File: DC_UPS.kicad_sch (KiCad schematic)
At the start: 32 parts, among them J1 USB_B_Micro, J2 POWER, J3 STATUS, Q1 SIS402DN, Q2 SIS402DN, U1 LTC4040

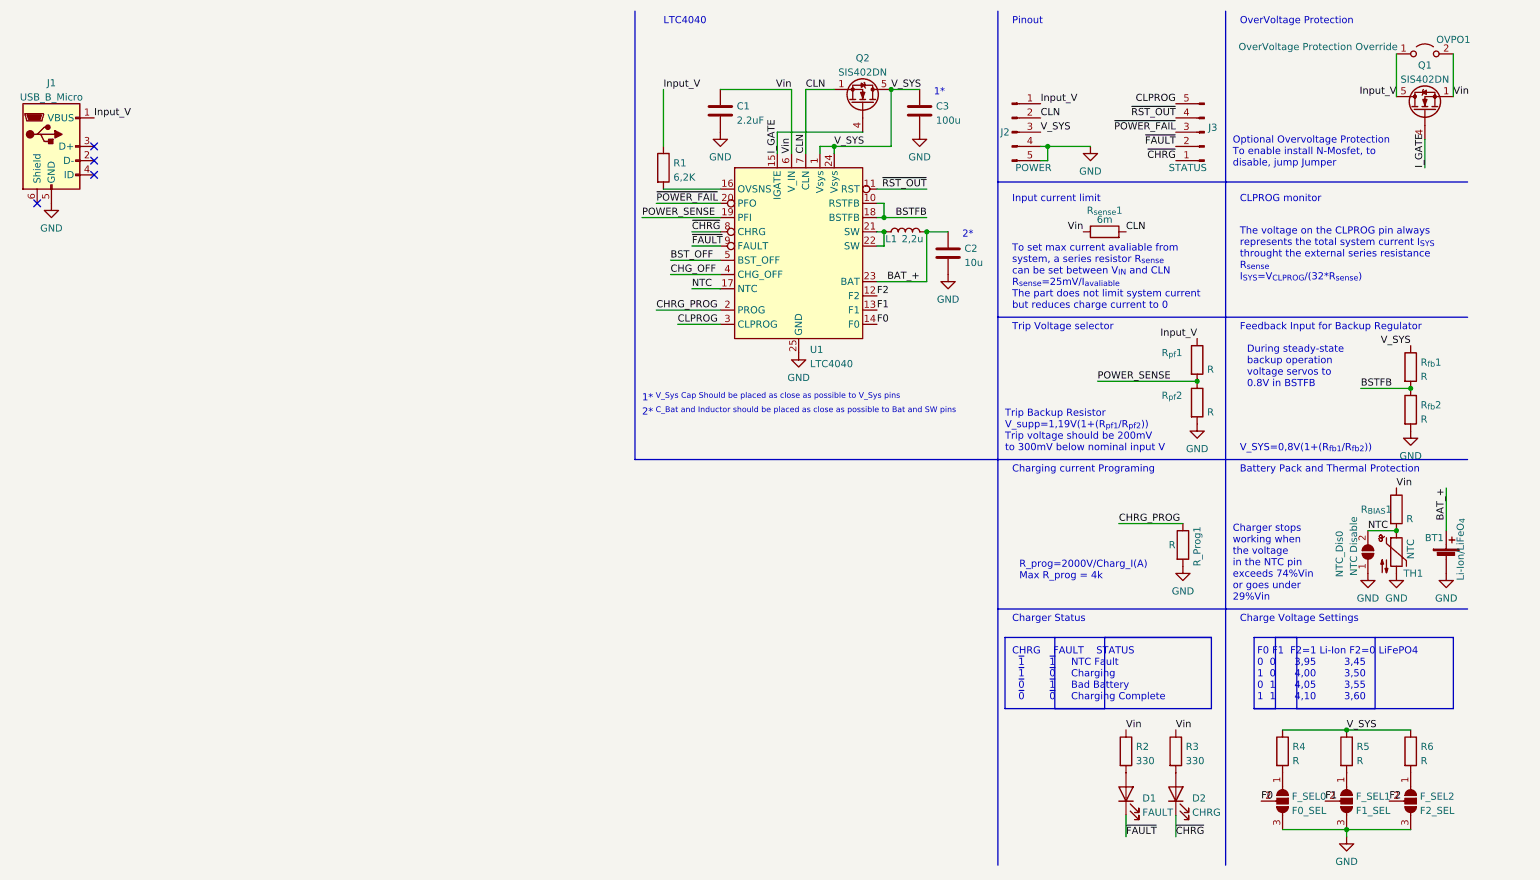
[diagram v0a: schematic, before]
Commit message: [Board]Build board without connectors
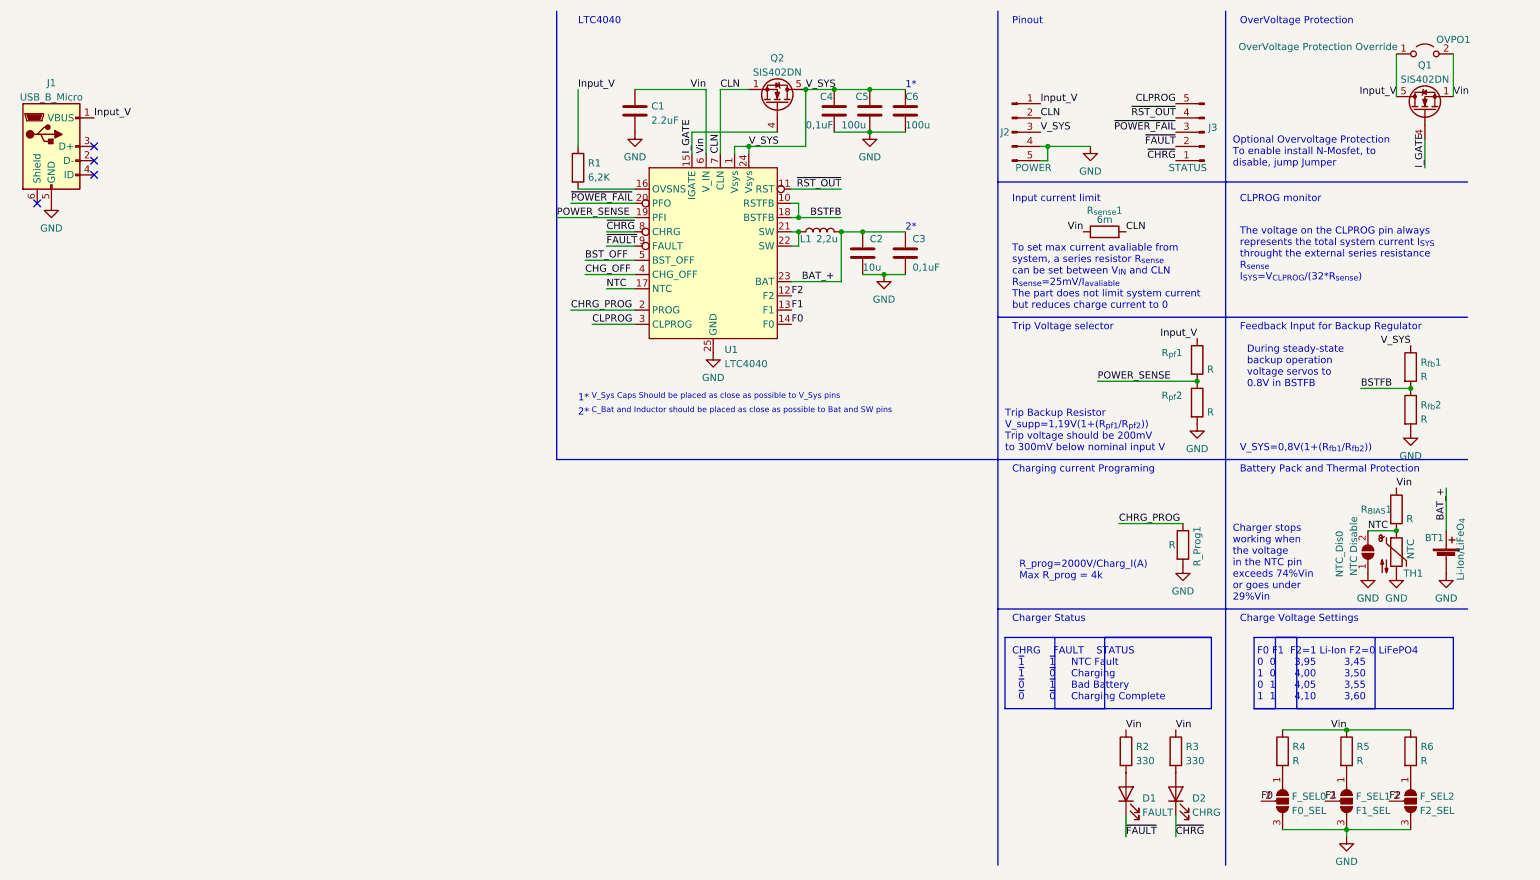
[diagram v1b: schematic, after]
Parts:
- added C3, C4: 0,1uF, Capacitor_SMD:C_0402_1005Metric_Pad0.74x0.62mm_HandSolder, symbol Device:C
- added C6: 100u, Capacitor_SMD:C_1206_3216Metric_Pad1.33x1.80mm_HandSolder, symbol Device:C
- renumbered C3 to C5
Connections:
- net BAT_+: now also C3.1
- net GND: now also C3.2, C4.2, C6.2
- net V_SYS: now also C4.1, C6.1; no longer R4.1, R5.1, R6.1
- net Vin: now also R4.1, R5.1, R6.1
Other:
- note added: "1*^{ V_Sys Caps Should be placed as close as possible to V_Sys pins}"
- note removed: "1*^{ V_Sys Cap Should be placed as close as possible to V_Sys pins}"
- moved on the sheet: C1, C2, C5, L1, Q2, R1, U1

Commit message: [Board]Finish product rev 1
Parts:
- added J4: BAT_CONN, Connector_JST:JST_SH_BM03B-SRSS-TB_1x03-1MP_P1.00mm_Vertical, symbol Connector:Conn_01x03_Female
- BT1: footprint Battery:BatteryHolder_Keystone_1042_1x18650 -> TE:TE_1776119-2
- J2, J3: footprint Connector_PinSocket_2.54mm:PinSocket_1x05_P2.54mm_Vertical -> Castellated_Header:CastellatedPinHeader_2.54mm_5
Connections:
- net BAT_+: now also J4.1 (Pin_1)
- net CLPROG: now also J3.4 (Pin_4); no longer J3.5 (Pin_5)
- net GND: now also J4.3 (Pin_3)
- net NTC: now also J4.2 (Pin_2)
- net ~{CHRG}: now also J3.2 (Pin_2); no longer J3.1 (Pin_1)
- net ~{FAULT}: now also J3.1 (Pin_1); no longer J3.2 (Pin_2)
- net ~{POWER_FAIL}: now also J3.5 (Pin_5); no longer J3.3 (Pin_3)
- net ~{RST_OUT}: now also J3.3 (Pin_3); no longer J3.4 (Pin_4)
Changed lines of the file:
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@@
+    (stroke (width 0) (type default) (color 0 0 0 0))
+  )
+  (wire (pts (xy 257.81 102.87) (xy 259.08 102.87))
     (stroke (width 0) (type default) (color 0 0 0 0))
   )
@@
     (effects (font (size 1.27 1.27)) (justify left bottom))
   )
-  (label "CLPROG" (at 232.41 29.21 180)
+  (label "CLPROG" (at 232.41 31.75 180)
     (effects (font (size 1.27 1.27)) (justify right bottom))
   )
@@
     (effects (font (size 1.27 1.27)) (justify left bottom))
   )
+  (label "NTC" (at 257.81 100.33 0)
+    (effects (font (size 1.27 1.27)) (justify left bottom))
+  )
+  (label "BAT_+" (at 257.81 97.79 0)
+    (effects (font (size 1.27 1.27)) (justify left bottom))
+  )
   (label "CLPROG" (at 128.27 68.58 0)
     (effects (font (size 1.27 1.27)) (justify left bottom))
@@
     (effects (font (size 1.27 1.27)) (justify left bottom))
   )
-  (label "~{CHRG}" (at 232.41 39.37 180)
+  (label "~{CHRG}" (at 232.41 36.83 180)
     (effects (font (size 1.27 1.27)) (justify right bottom))
   )
@@
     (effects (font (size 1.27 1.27)) (justify right bottom))
   )
-  (label "~{FAULT}" (at 232.41 36.83 180)
+  (label "~{FAULT}" (at 232.41 39.37 180)
     (effects (font (size 1.27 1.27)) (justify right bottom))
   )
@@
     (effects (font (size 1.27 1.27)) (justify left bottom))
   )
-  (label "~{POWER_FAIL}" (at 232.41 34.29 180)
+  (label "~{POWER_FAIL}" (at 232.41 29.21 180)
     (effects (font (size 1.27 1.27)) (justify right bottom))
   )
@@
     (effects (font (size 1.27 1.27)) (justify right bottom))
   )
-  (label "~{RST_OUT}" (at 232.41 31.75 180)
+  (label "~{RST_OUT}" (at 232.41 34.29 180)
     (effects (font (size 1.27 1.27)) (justify right bottom))
   )
@@
       (effects (font (size 1.27 1.27)) (justify left))
     )
-    (property "Footprint" "Battery:BatteryHolder_Keystone_1042_1x18650" (id 2) (at 280.67 108.966 90)
+    (property "Footprint" "TE:TE_1776119-2" (id 2) (at 280.67 108.966 90)
       (effects (font (size 1.27 1.27)) hide)
     )
@@
     (property "Reference" "J2" (id 0) (at 201.93 34.29 0))
     (property "Value" "POWER" (id 1) (at 207.01 40.64 0))
-    (property "Footprint" "Connector_PinSocket_2.54mm:PinSocket_1x05_P2.54mm_Vertical" (id 2) (at 203.2 34.29 0)
+    (property "Footprint" "Castellated_Header:CastellatedPinHeader_2.54mm_5" (id 2) (at 203.2 34.29 0)
       (effects (font (size 1.27 1.27)) hide)
     )
@@
     (pin "2")
   )
+  (symbol (lib_id "power:GND") (at 259.08 102.87 0) (unit 1)
+    (in_bom yes) (on_board yes) (fields_autoplaced)
+    (property "Reference" "#PWR011" (id 0) (at 259.08 109.22 0)
+      (effects (font (size 1.27 1.27)) hide)
+    )
+    (property "Value" "GND" (id 1) (at 259.08 107.3134 0))
+    (property "Footprint" "" (id 2) (at 259.08 102.87 0)
+      (effects (font (size 1.27 1.27)) hide)
+    )
+    (property "Datasheet" "" (id 3) (at 259.08 102.87 0)
+      (effects (font (size 1.27 1.27)) hide)
+    )
+    (pin "1")
+  )
   (symbol (lib_id "power:GND") (at 180.34 59.69 0) (unit 1)
     (in_bom yes) (on_board yes) (fields_autoplaced)
@@
     (pin "1")
     (pin "2")
+  )
+  (symbol (lib_id "Connector:Conn_01x03_Female") (at 252.73 100.33 0) (mirror y) (unit 1)
+    (in_bom yes) (on_board yes)
+    (property "Reference" "J4" (id 0) (at 250.19 102.87 0))
+    (property "Value" "BAT_CONN" (id 1) (at 247.65 99.06 0))
+    (property "Footprint" "Connector_JST:JST_SH_BM03B-SRSS-TB_1x03-1MP_P1.00mm_Vertical" (id 2) (at 252.73 100.33 0)
+      (effects (font (size 1.27 1.27)) hide)
+    )
+    (property "Datasheet" "~" (id 3) (at 252.73 100.33 0)
+      (effects (font (size 1.27 1.27)) hide)
+    )
+    (pin "1")
+    (pin "2")
+    (pin "3")
   )
   (symbol (lib_id "Device:R") (at 274.32 83.82 0) (unit 1)
@@
       (effects (font (size 1.27 1.27)) (justify right))
     )
-    (property "Footprint" "Connector_PinSocket_2.54mm:PinSocket_1x05_P2.54mm_Vertical" (id 2) (at 237.49 34.29 0)
+    (property "Footprint" "Castellated_Header:CastellatedPinHeader_2.54mm_5" (id 2) (at 237.49 34.29 0)
       (effects (font (size 1.27 1.27)) hide)
     )
@@
       (reference "#PWR010") (unit 1) (value "GND") (footprint "")
     )
+    (path "/831bf088-8c46-425e-916a-58cc9ad46bab"
+      (reference "#PWR011") (unit 1) (value "GND") (footprint "")
+    )
     (path "/7340f23f-79f5-4b3d-8131-c749ccb9adb7"
       (reference "#PWR0101") (unit 1) (value "GND") (footprint "")
@@
     )
     (path "/1fe1231d-b489-4d88-bb46-c8ef52336c04"
-      (reference "BT1") (unit 1) (value "Li-Ion/LiFeO_{4}") (footprint "Battery:BatteryHolder_Keystone_1042_1x18650")
+      (reference "BT1") (unit 1) (value "Li-Ion/LiFeO_{4}") (footprint "TE:TE_1776119-2")
     )
     (path "/16108561-d524-4af7-aebe-99ff2f7b86ac"
@@
     )
     (path "/770479ce-0e0c-48db-aa93-4f707effabb5"
-      (reference "J2") (unit 1) (value "POWER") (footprint "Connector_PinSocket_2.54mm:PinSocket_1x05_P2.54mm_Vertical")
+      (reference "J2") (unit 1) (value "POWER") (footprint "Castellated_Header:CastellatedPinHeader_2.54mm_5")
     )
     (path "/f4ba0e0f-7b19-403d-a325-a6a1d50c7d84"
-      (reference "J3") (unit 1) (value "STATUS") (footprint "Connector_PinSocket_2.54mm:PinSocket_1x05_P2.54mm_Vertical")
+      (reference "J3") (unit 1) (value "STATUS") (footprint "Castellated_Header:CastellatedPinHeader_2.54mm_5")
+    )
+    (path "/b3ce3a3c-15dd-408a-98e3-2629b485e19a"
+      (reference "J4") (unit 1) (value "BAT_CONN") (footprint "Connector_JST:JST_SH_BM03B-SRSS-TB_1x03-1MP_P1.00mm_Vertical")
     )
     (path "/50cd8e16-04be-40d8-917e-710c4d59ecf8"

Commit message: [Board][Readme]Update
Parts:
- C3: renamed from C2; footprint Capacitor_SMD:C_0402_1005Metric_Pad0.74x0.62mm_HandSolder -> Capacitor_SMD:C_0805_2012Metric_Pad1.18x1.45mm_HandSolder
- renumbered C3 to C2
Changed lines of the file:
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@@
   (symbol (lib_id "Device:C") (at 176.53 55.88 0) (unit 1)
     (in_bom yes) (on_board yes)
-    (property "Reference" "C2" (id 0) (at 177.8 53.34 0)
+    (property "Reference" "C3" (id 0) (at 177.8 53.34 0)
       (effects (font (size 1.27 1.27)) (justify left))
     )
@@
       (effects (font (size 1.27 1.27)) (justify left))
     )
-    (property "Footprint" "Capacitor_SMD:C_0402_1005Metric_Pad0.74x0.62mm_HandSolder" (id 2) (at 177.4952 59.69 0)
+    (property "Footprint" "Capacitor_SMD:C_0805_2012Metric_Pad1.18x1.45mm_HandSolder" (id 2) (at 177.4952 59.69 0)
       (effects (font (size 1.27 1.27)) hide)
     )
@@
   (symbol (lib_id "Device:C") (at 184.15 55.88 0) (unit 1)
     (in_bom yes) (on_board yes)
-    (property "Reference" "C3" (id 0) (at 185.42 53.34 0)
+    (property "Reference" "C2" (id 0) (at 185.42 53.34 0)
       (effects (font (size 1.27 1.27)) (justify left))
     )
@@
       (reference "C1") (unit 1) (value "2.2uF") (footprint "Capacitor_SMD:C_0402_1005Metric_Pad0.74x0.62mm_HandSolder")
     )
+    (path "/64f276de-1c7a-4ff7-8974-d21304c4ffe2"
+      (reference "C2") (unit 1) (value "0,1uF") (footprint "Capacitor_SMD:C_0402_1005Metric_Pad0.74x0.62mm_HandSolder")
+    )
     (path "/36eeaafd-4e85-4cfc-9f34-4ad5bfce35a3"
-      (reference "C2") (unit 1) (value "10u") (footprint "Capacitor_SMD:C_0402_1005Metric_Pad0.74x0.62mm_HandSolder")
-    )
-    (path "/64f276de-1c7a-4ff7-8974-d21304c4ffe2"
-      (reference "C3") (unit 1) (value "0,1uF") (footprint "Capacitor_SMD:C_0402_1005Metric_Pad0.74x0.62mm_HandSolder")
+      (reference "C3") (unit 1) (value "10u") (footprint "Capacitor_SMD:C_0805_2012Metric_Pad1.18x1.45mm_HandSolder")
     )
     (path "/4d0223b3-ce78-4ac4-bfe6-79ff18ec7346"
